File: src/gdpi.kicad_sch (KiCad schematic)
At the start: 24 parts, among them J7 HDMI_C_1.3, U1 ECP5U_12_CABGA256, U9 PCA9306DC1, Y1 ECS-2520MV-xxx-xx

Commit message: Rev 2
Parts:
- C13, C14, C15, C16, C17, C18, C19, C20: footprint Capacitor_SMD:C_0603_1608Metric -> Capacitor_SMD:C_0402_1005Metric; LCSC Part (none) -> C1532
- C21: LCSC Part (none) -> C14858
- C23, C39: LCSC Part (none) -> C1525
- C40: value 15pF -> 5pF; LCSC Part (none) -> C541339
- R10, R8: LCSC Part (none) -> C23179
- R11: LCSC Part (none) -> C25803
- R12, R13: LCSC Part (none) -> C23162
- R14, R15: LCSC Part (none) -> C22978
- R9: LCSC Part (none) -> C25804
- U9: LCSC Part (none) -> C129510
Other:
- note added: "Shift 3v3 to 5v"
- moved on the sheet: C13, C14, C15, C16, C17, C18, C19, C20, C21, C39, C40, J7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

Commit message: Tidy project
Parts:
- C13, C14, C15, C16, C17, C18, C19, C20: JLCPCB Part # (none) -> C1532; LCSC Part C1532 -> (none)
- C21: JLCPCB Part # (none) -> C14858; LCSC Part C14858 -> (none)
- C23, C39: JLCPCB Part # (none) -> C1525; LCSC Part C1525 -> (none)
- C40: JLCPCB Part # (none) -> C541339; LCSC Part C541339 -> (none)
- J7: JLCPCB Part # (none) -> C2682170; LCSC Part C2682170 -> (none)
- R10, R8: JLCPCB Part # (none) -> C23179; LCSC Part C23179 -> (none)
- R11: JLCPCB Part # (none) -> C25803; LCSC Part C25803 -> (none)
- R12, R13: JLCPCB Part # (none) -> C23162; LCSC Part C23162 -> (none)
- R14, R15: JLCPCB Part # (none) -> C22978; LCSC Part C22978 -> (none)
- R9: JLCPCB Part # (none) -> C25804; LCSC Part C25804 -> (none)
- U1: JLCPCB Part # (none) -> C1521614; LCSC Part C1521614 -> (none)
- U9: JLCPCB Part # (none) -> C129510; LCSC Part C129510 -> (none)
- Y1: JLCPCB Part # (none) -> C5189451; LCSC Part C5189451 -> (none)
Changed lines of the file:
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@@
 			)
 		)
-		(property "LCSC Part" "C25803"
+		(property "JLCPCB Part #" "C25803"
 			(at 158.75 109.22 0)
 			(effects
@@
 			)
 		)
-		(property "LCSC Part" "C23162"
+		(property "JLCPCB Part #" "C23162"
 			(at 163.83 109.22 0)
 			(effects
@@
 			)
 		)
-		(property "LCSC Part" "C23162"
+		(property "JLCPCB Part #" "C23162"
 			(at 168.91 109.22 0)
 			(effects
@@
 			)
 		)
-		(property "LCSC Part" "C14858"
+		(property "JLCPCB Part #" "C14858"
 			(at 158.75 139.7 0)
 			(effects
@@
 			)
 		)
-		(property "LCSC Part" "C22978"
+		(property "JLCPCB Part #" "C22978"
 			(at 132.08 121.92 0)
 			(effects
@@
 			)
 		)
-		(property "LCSC Part" "C22978"
+		(property "JLCPCB Part #" "C22978"
 			(at 128.27 121.92 0)
 			(effects
@@
 			)
 		)
-		(property "LCSC Part" "C23179"
+		(property "JLCPCB Part #" "C23179"
 			(at 226.06 140.97 0)
 			(effects
@@
 			)
 		)
-		(property "LCSC Part" "C2682170 "
+		(property "JLCPCB Part #" "C2682170 "
 			(at 259.08 123.19 0)
 			(effects
@@
 					(size 1.27 1.27)
 				)
-				(hide yes)
 			)
 		)
@@
 			)
 		)
-		(property "LCSC Part" "C1532"
+		(property "JLCPCB Part #" "C1532"
 			(at 226.06 107.95 0)
 			(effects
@@
 			)
 		)
-		(property "LCSC Part" "C1532"
+		(property "JLCPCB Part #" "C1532"
 			(at 237.49 120.65 0)
 			(effects
@@
 			)
 		)
-		(property "LCSC Part" "C1532"
+		(property "JLCPCB Part #" "C1532"
 			(at 237.49 115.57 0)
 			(effects
@@
 			)
 		)
-		(property "LCSC Part" "C1525"
+		(property "JLCPCB Part #" "C1525"
 			(at 72.39 35.56 0)
 			(effects
@@
 					(size 1.27 1.27)
 				)
-				(hide yes)
 			)
 		)
@@
 			)
 		)
-		(property "LCSC Part" "C1532"
+		(property "JLCPCB Part #" "C1532"
 			(at 226.06 113.03 0)
 			(effects
@@
 			)
 		)
-		(property "LCSC Part" "C1532"
+		(property "JLCPCB Part #" "C1532"
 			(at 226.06 102.87 0)
 			(effects
@@
 					(size 1.27 1.27)
 				)
-				(hide yes)
 			)
 		)
@@
 			)
 		)
-		(property "LCSC Part" "C23179"
+		(property "JLCPCB Part #" "C23179"
 			(at 226.06 125.73 0)
 			(effects
@@
 			)
 		)
-		(property "LCSC Part" " C1521614"
+		(property "JLCPCB Part #" " C1521614"
 			(at 69.85 83.82 0)
 			(effects
@@
 					(size 1.27 1.27)
 				)
-				(hide yes)
 			)
 		)
@@
 			)
 		)
-		(property "LCSC Part" "C1532"
+		(property "JLCPCB Part #" "C1532"
 			(at 226.06 118.11 0)
 			(effects
@@
 			)
 		)
-		(property "LCSC Part" "C1532"
+		(property "JLCPCB Part #" "C1532"
 			(at 237.49 110.49 0)
 			(effects
@@
 			)
 		)
-		(property "LCSC Part" "C25804"
+		(property "JLCPCB Part #" "C25804"
 			(at 226.06 138.43 0)
 			(effects
@@
 			)
 		)
-		(property "LCSC Part" " C5189451"
+		(property "JLCPCB Part #" " C5189451"
 			(at 148.59 64.77 0)
 			(effects
@@
 					(size 1.27 1.27)
 				)
-				(hide yes)
 			)
 		)
@@
 			)
 		)
-		(property "LCSC Part" "C541339"
+		(property "JLCPCB Part #" "C541339"
 			(at 160.02 68.58 0)
 			(effects
@@
 					(size 1.27 1.27)
 				)
-				(hide yes)
 			)
 		)
@@
 			)
 		)
-		(property "LCSC Part" "C129510"
+		(property "JLCPCB Part #" "C129510"
 			(at 144.78 130.81 0)
 			(effects
@@
 			)
 		)
-		(property "LCSC Part" "C1532"
+		(property "JLCPCB Part #" "C1532"
 			(at 237.49 105.41 0)
 			(effects
@@
 			)
 		)
-		(property "LCSC Part" "C1525"
+		(property "JLCPCB Part #" "C1525"
 			(at 134.62 64.77 0)
 			(effects
@@
 					(size 1.27 1.27)
 				)
-				(hide yes)
-			)
-		)
+			)
+		)

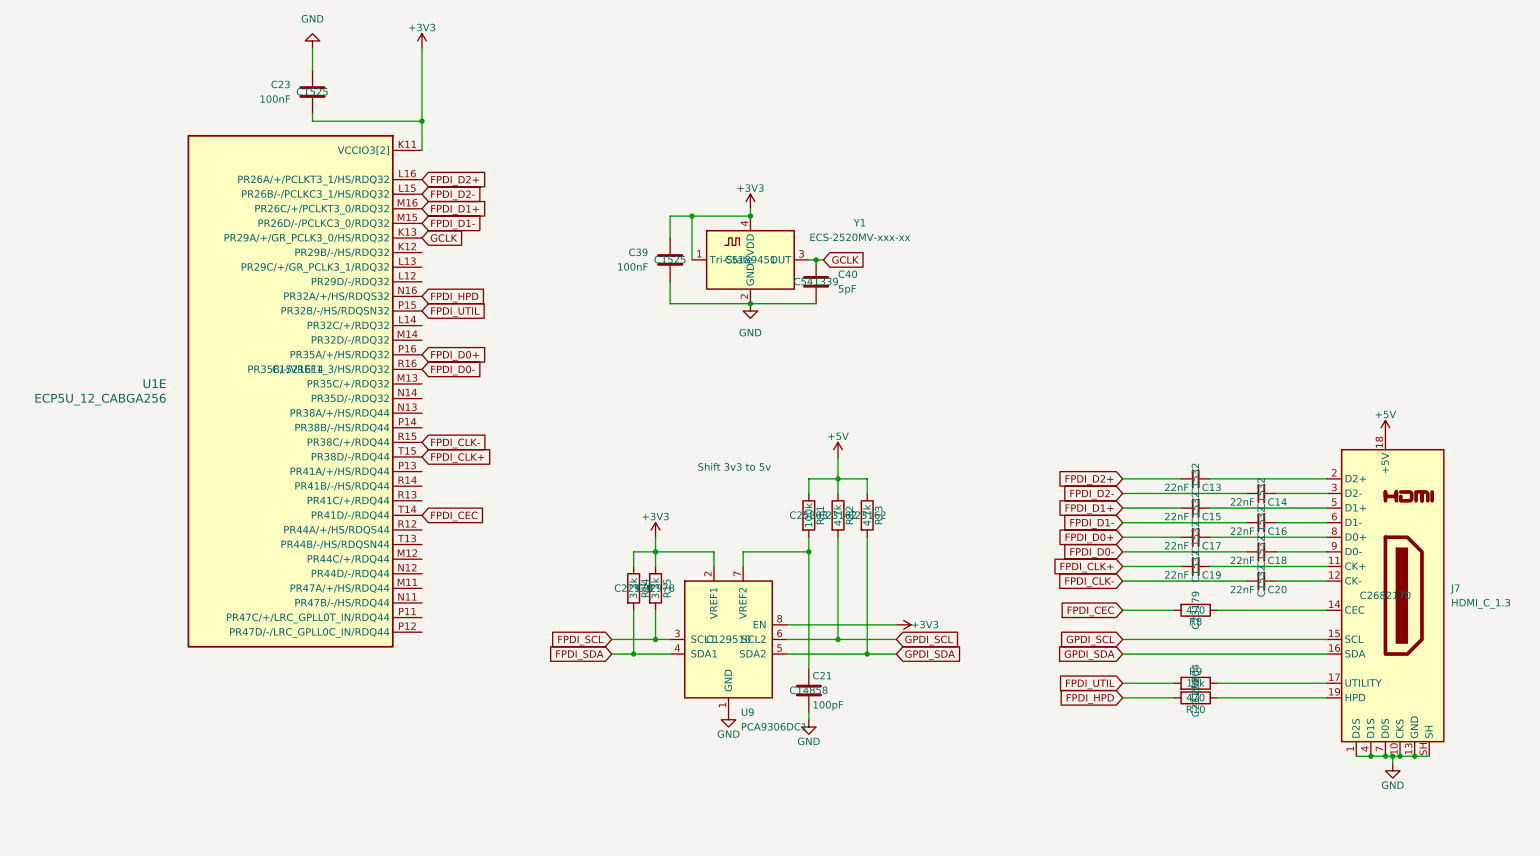
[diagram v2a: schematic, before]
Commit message: Add test points
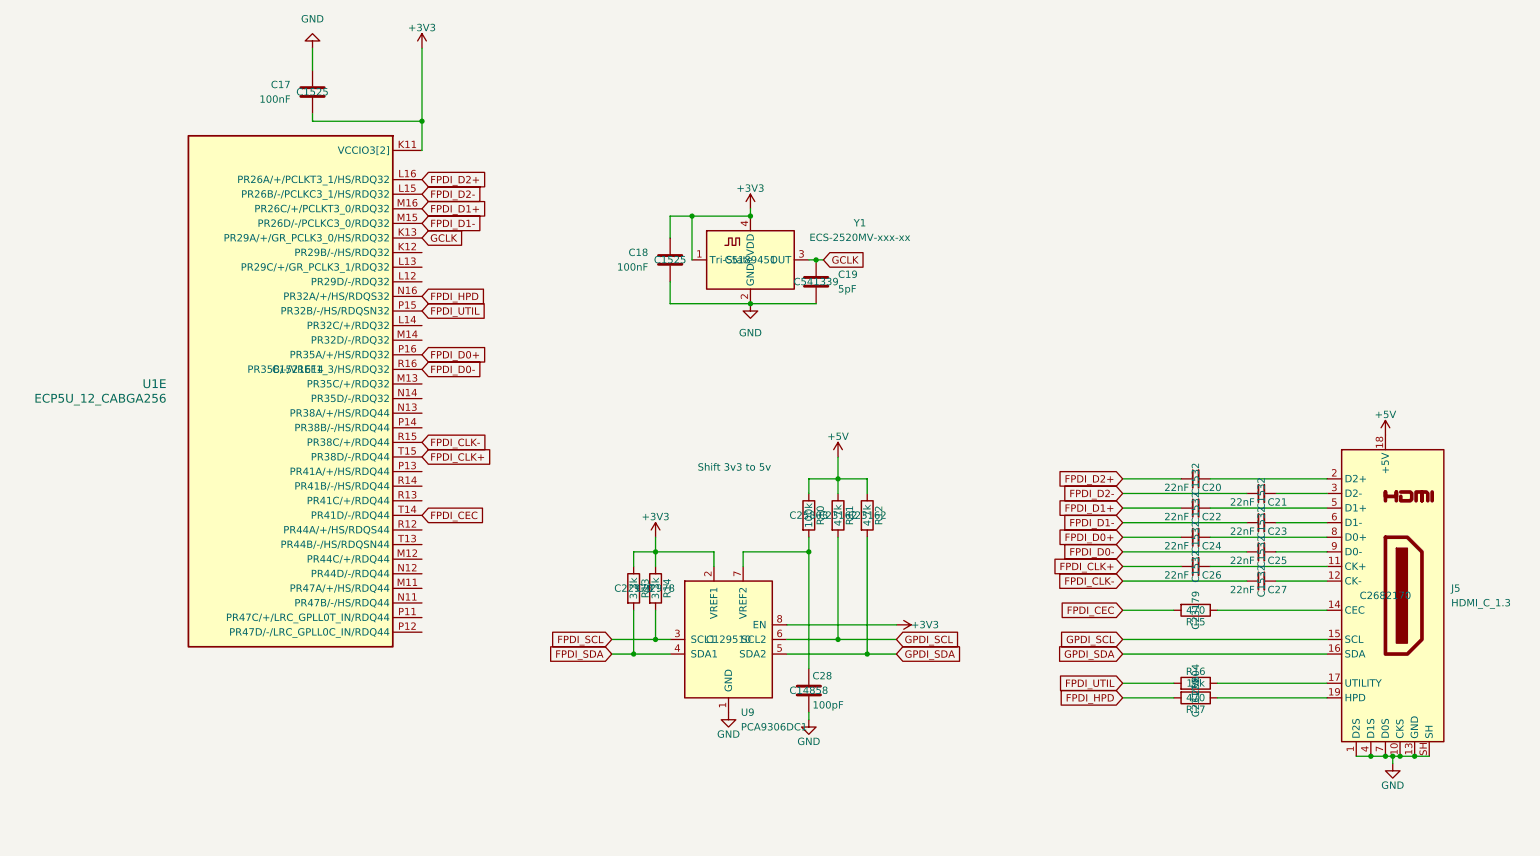
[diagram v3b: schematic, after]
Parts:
- renumbered C23 to C17, C39 to C18, C40 to C19, C13 to C20, C14 to C21, C15 to C22, C16 to C23, C17 to C24, C18 to C25, C19 to C26, C20 to C27, C21 to C28, J7 to J5, R11 to R10, R12 to R11, R13 to R12, R14 to R13, R15 to R14, R8 to R15, R9 to R16, R10 to R17
